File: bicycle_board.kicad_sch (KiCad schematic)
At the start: 73 parts, among them J1 Micro_SD_Card, J10 USB_A, J11 Conn_01x04, J12 Conn_01x01, J13 Conn_01x04, J14 Conn_01x01, J2 USB_C_Receptacle_USB2.0_16P, J5 Conn_01x08, J6 Conn_01x04, J7 Conn_01x05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

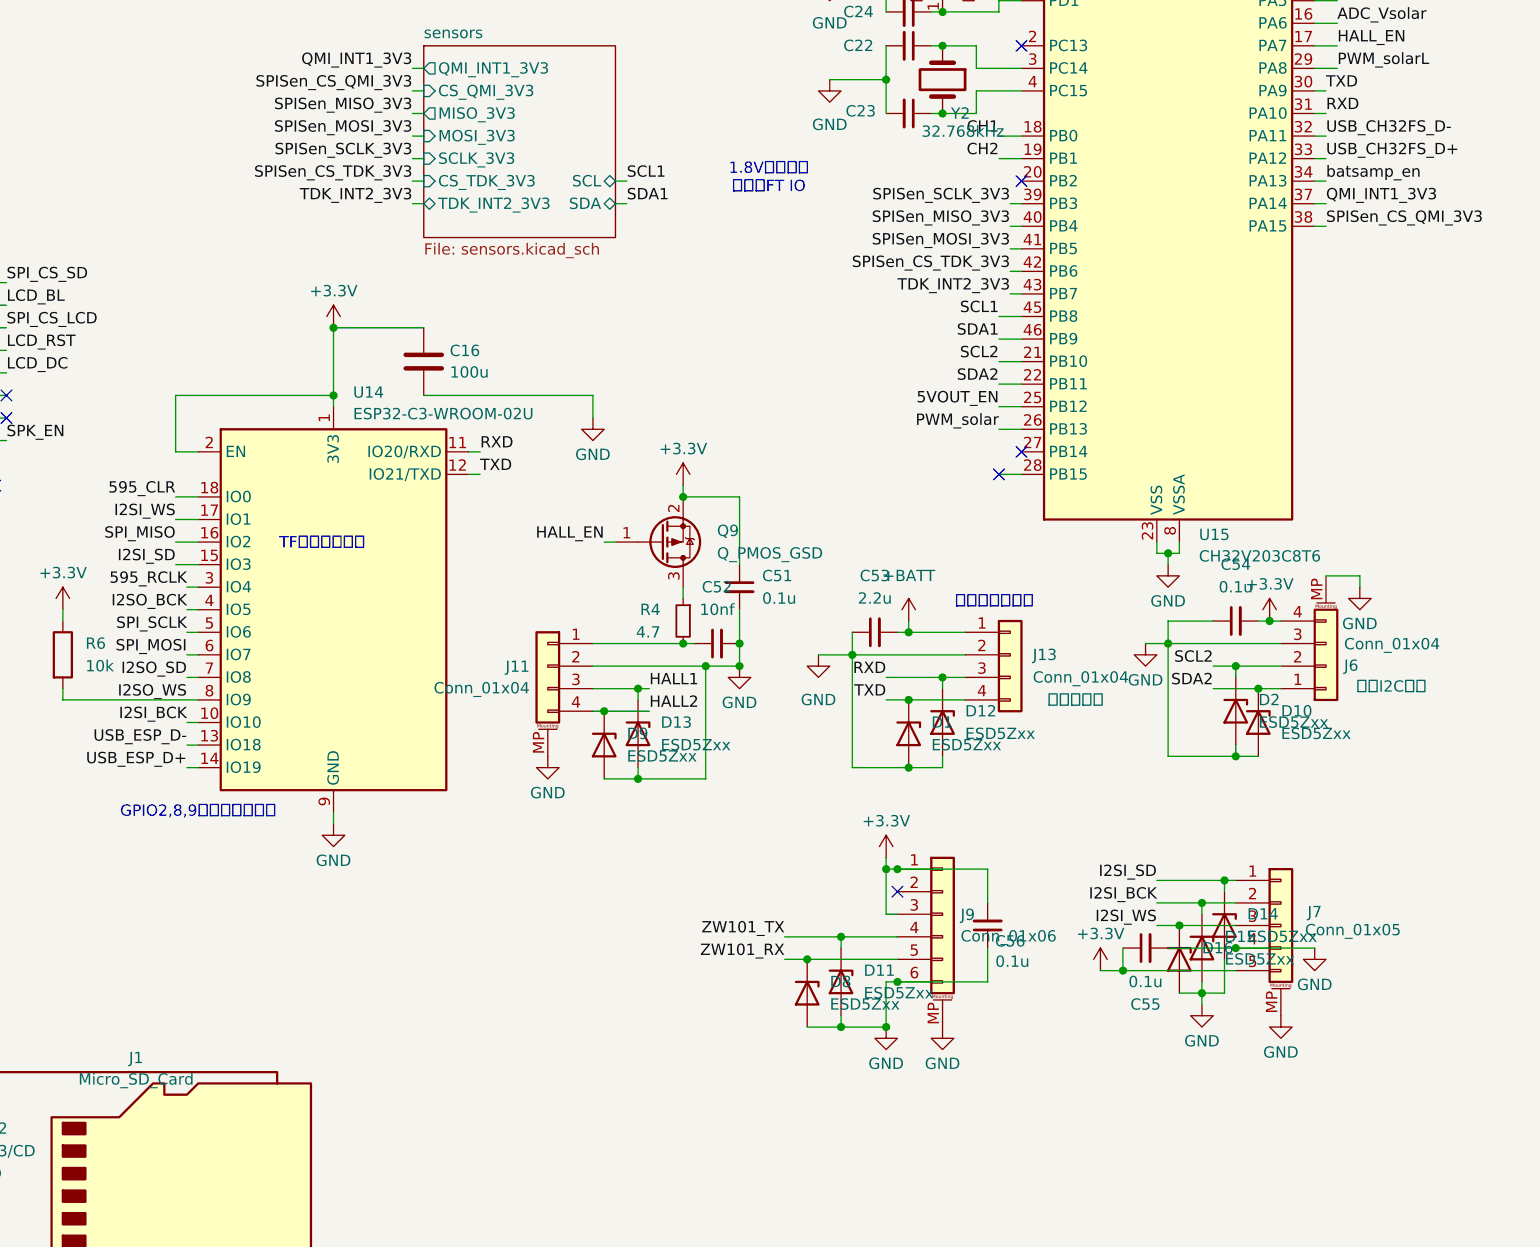
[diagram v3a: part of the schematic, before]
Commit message: 添加FRAM储存器
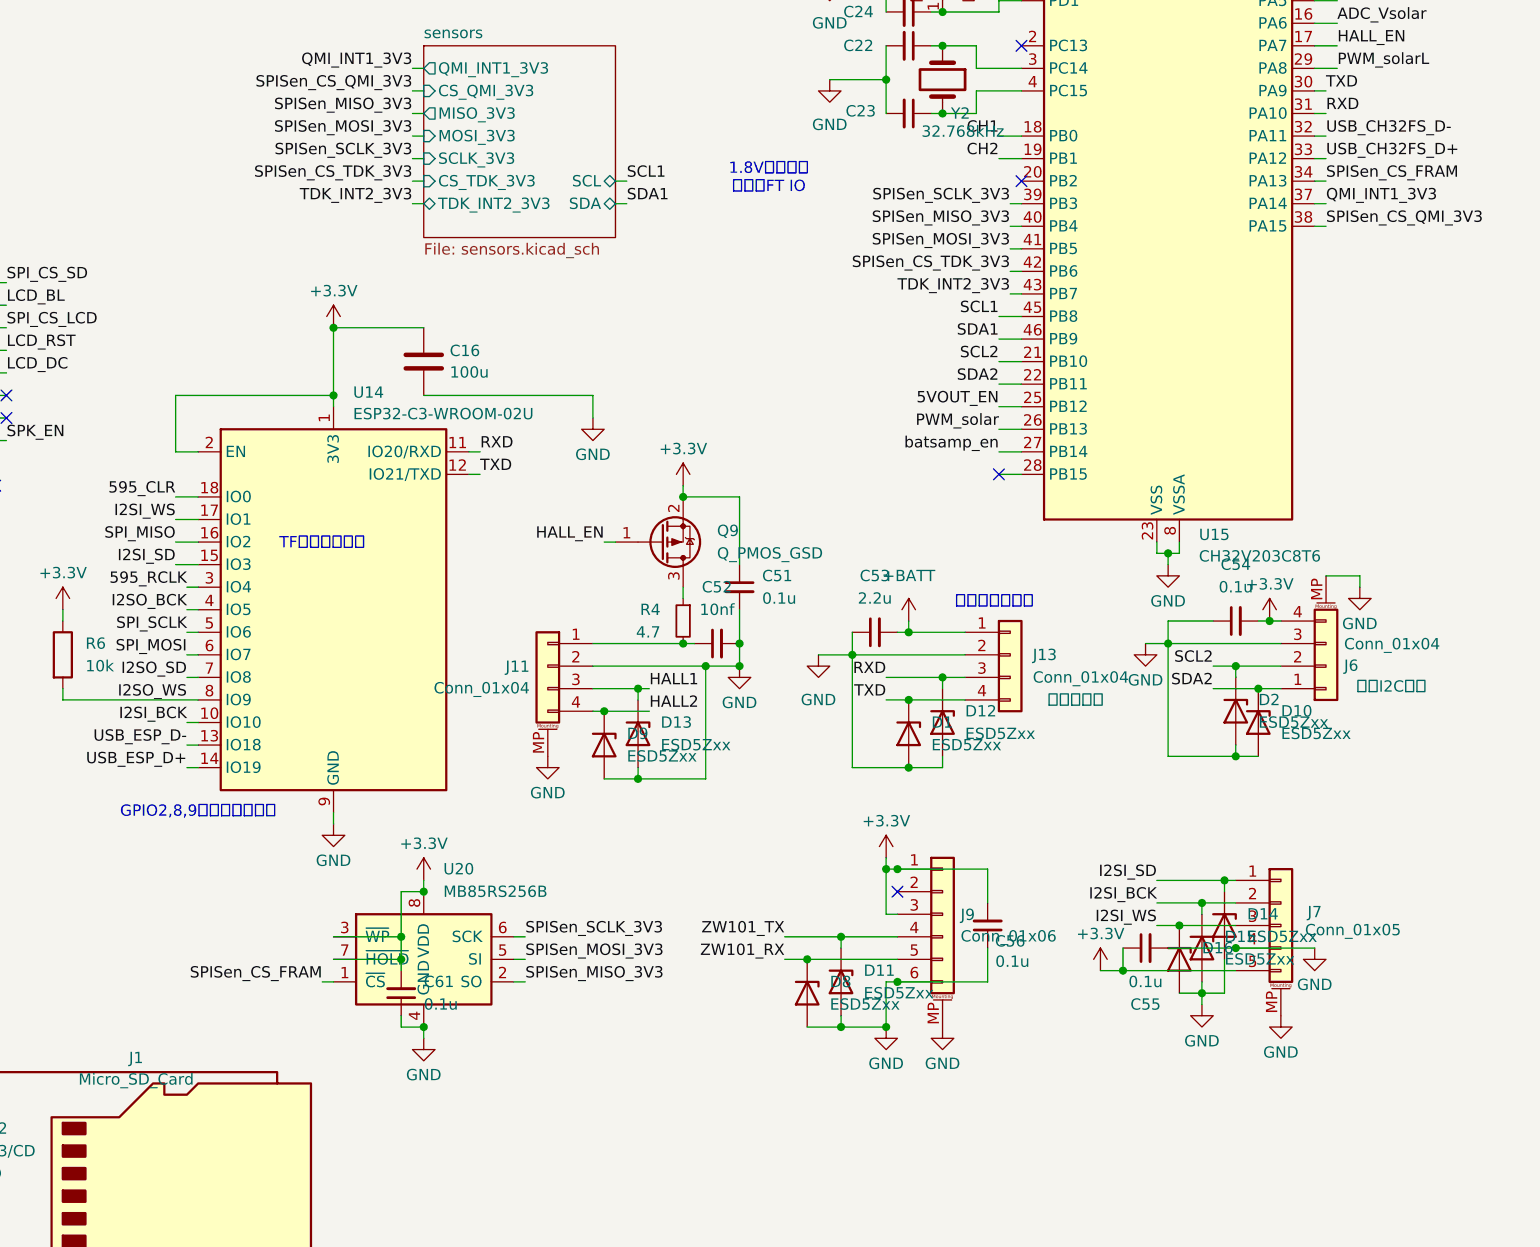
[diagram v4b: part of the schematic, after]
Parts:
- added C61: 0.1u, Capacitor_SMD:C_0402_1005Metric, symbol Device:C_Small
- added U20: MB85RS256B, Package_SO:SSOP-8_3.9x5.05mm_P1.27mm, symbol Memory_NVRAM:MB85RS256B
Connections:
- net +3.3V: now also C61.2, U20.3 (~{WP}), U20.7 (~{HOLD}), U20.8 (VDD)
- net GND: now also C61.1, U20.4 (GND)
- net SPISen_MISO_3V3: now also U20.2 (SO)
- net SPISen_MOSI_3V3: now also U20.5 (SI)
- net SPISen_SCLK_3V3: now also U20.6 (SCK)
- net batsamp_en: now also U15.27 (PB14); no longer U15.34 (PA13)
- new net SPISen_CS_FRAM: U15.34 (PA13), U20.1 (~{CS})
- no-connect marks 15 -> 14
